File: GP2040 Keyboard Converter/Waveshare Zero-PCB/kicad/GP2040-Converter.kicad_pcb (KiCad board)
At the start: 2 copper layers, 30.4 x 68 mm, 12 parts, among them J1 USB_A, SW1 SW_Push_Open, SW2 SW_Push_Open, SW3 SW_Push_Open, SW4 SW_Push_Open, SW5 SW_Push_Open, SW6 SW_Push_Open

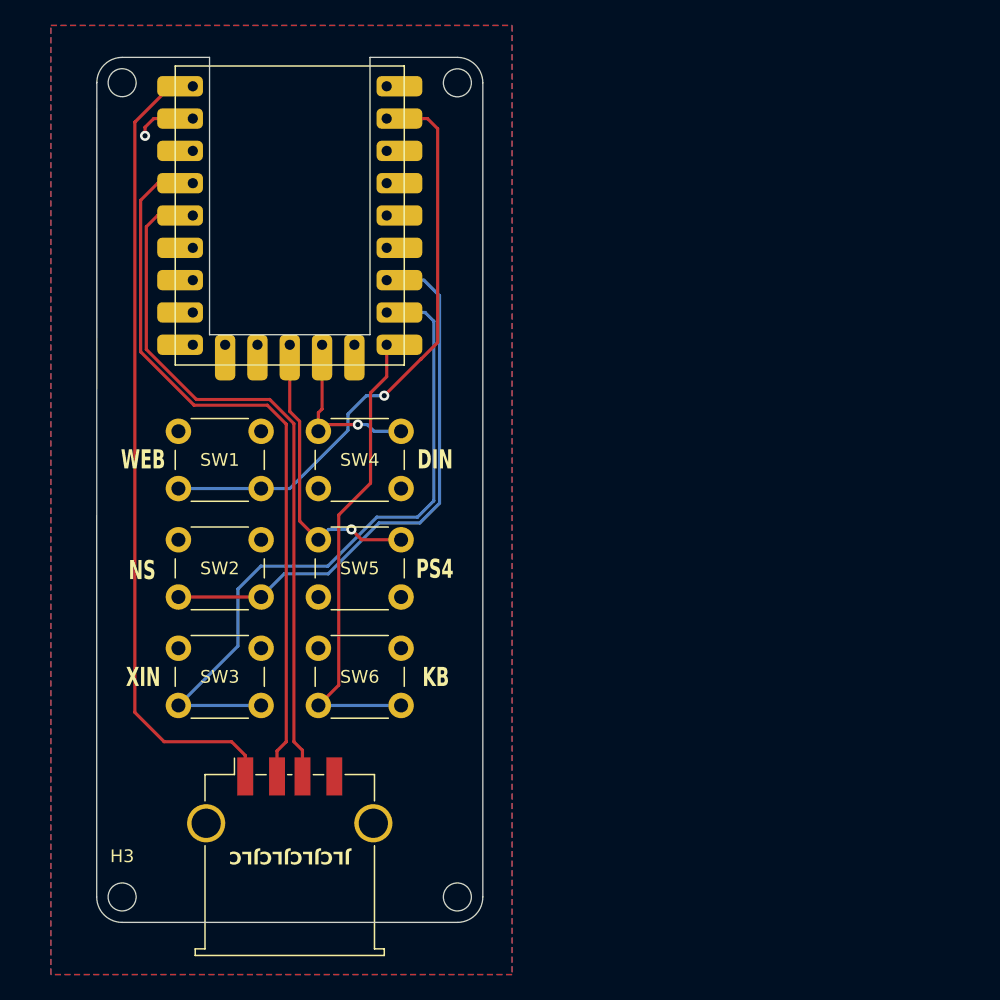
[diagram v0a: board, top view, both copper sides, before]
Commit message: Add GP2040 Logo to Waveshare Keyboard Converter
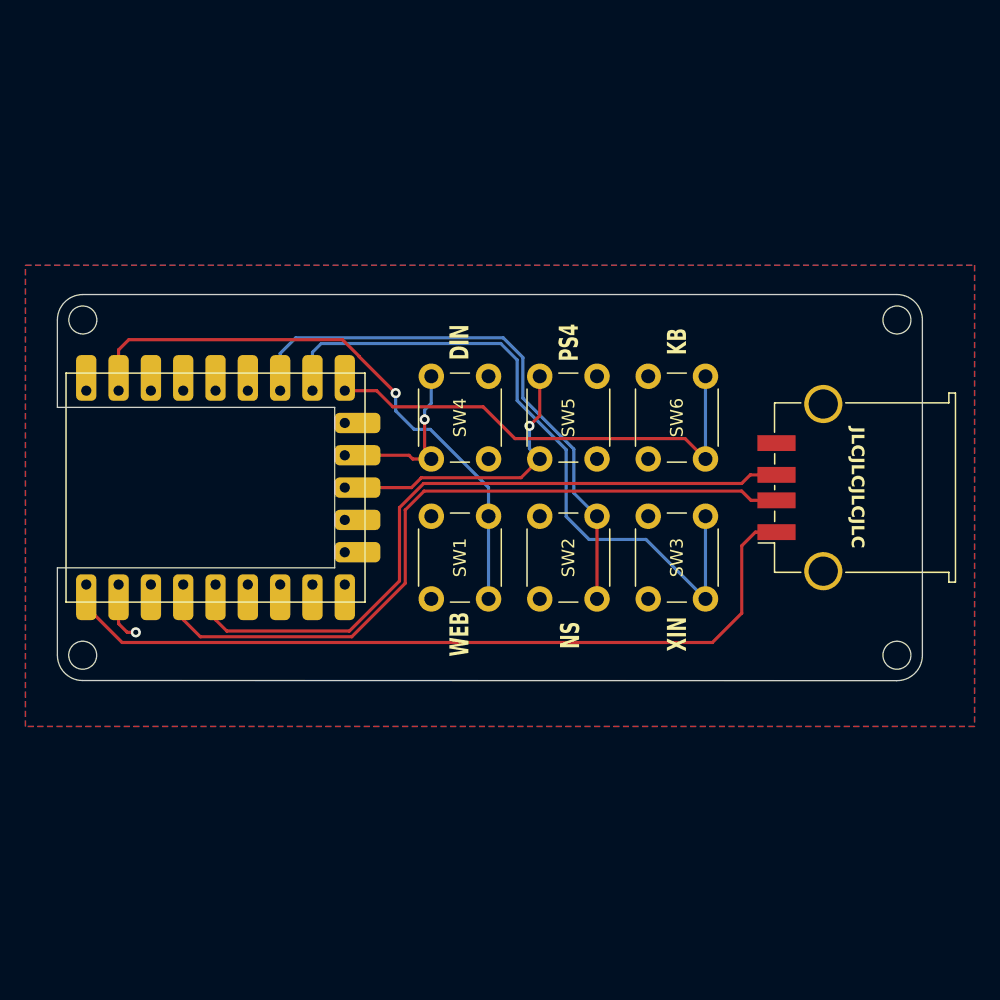
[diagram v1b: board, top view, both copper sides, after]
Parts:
- added G***: LOGO, Logo:gp2040-ce-logo-inside-BW, B.Cu at (77.8, 65.0)
- moved H3 63.8 mm to (97.8, 78.0), turned to 90 degrees
- moved H4 57.0 mm to (97.8, 51.6), turned to 90 degrees
- moved J1 53.3 mm to (94.7, 64.8), turned to 90 degrees
- moved H1 45.1 mm to (33.8, 78.0), turned to 90 degrees
- moved SW3 38.0 mm to (82.8, 67.1), turned to -90 degrees
- moved SW6 35.2 mm to (82.8, 56.1), turned to -90 degrees
- moved H2 34.8 mm to (33.8, 51.6), turned to 90 degrees
- moved SW2 27.2 mm to (74.2, 67.1), turned to -90 degrees
- moved RZ1 23.9 mm to (56.0, 73.8), turned to 90 degrees
- moved SW5 18.5 mm to (69.7, 62.6), turned to 90 degrees
- moved SW1 18.0 mm to (65.7, 67.1), turned to -90 degrees
- moved SW4 9.14 mm to (61.2, 62.6), turned to 90 degrees
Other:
- board size 30.4 x 68 mm -> 68 x 30.4 mm
